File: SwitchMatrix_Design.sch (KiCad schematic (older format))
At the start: 0 parts

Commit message: v1b
Main notes -
Switch matrix added however not finished.
Minor notes -
Backspace is the only modified key to have been created so far.
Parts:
- added D? (x202): D_Small, symbol Device:D_Small
- added MX? (x202): MX-NoLED, symbol MX_Alps_Hybrid:MX-NoLED
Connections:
- net labels added: row0
- wire segments 0 -> 229

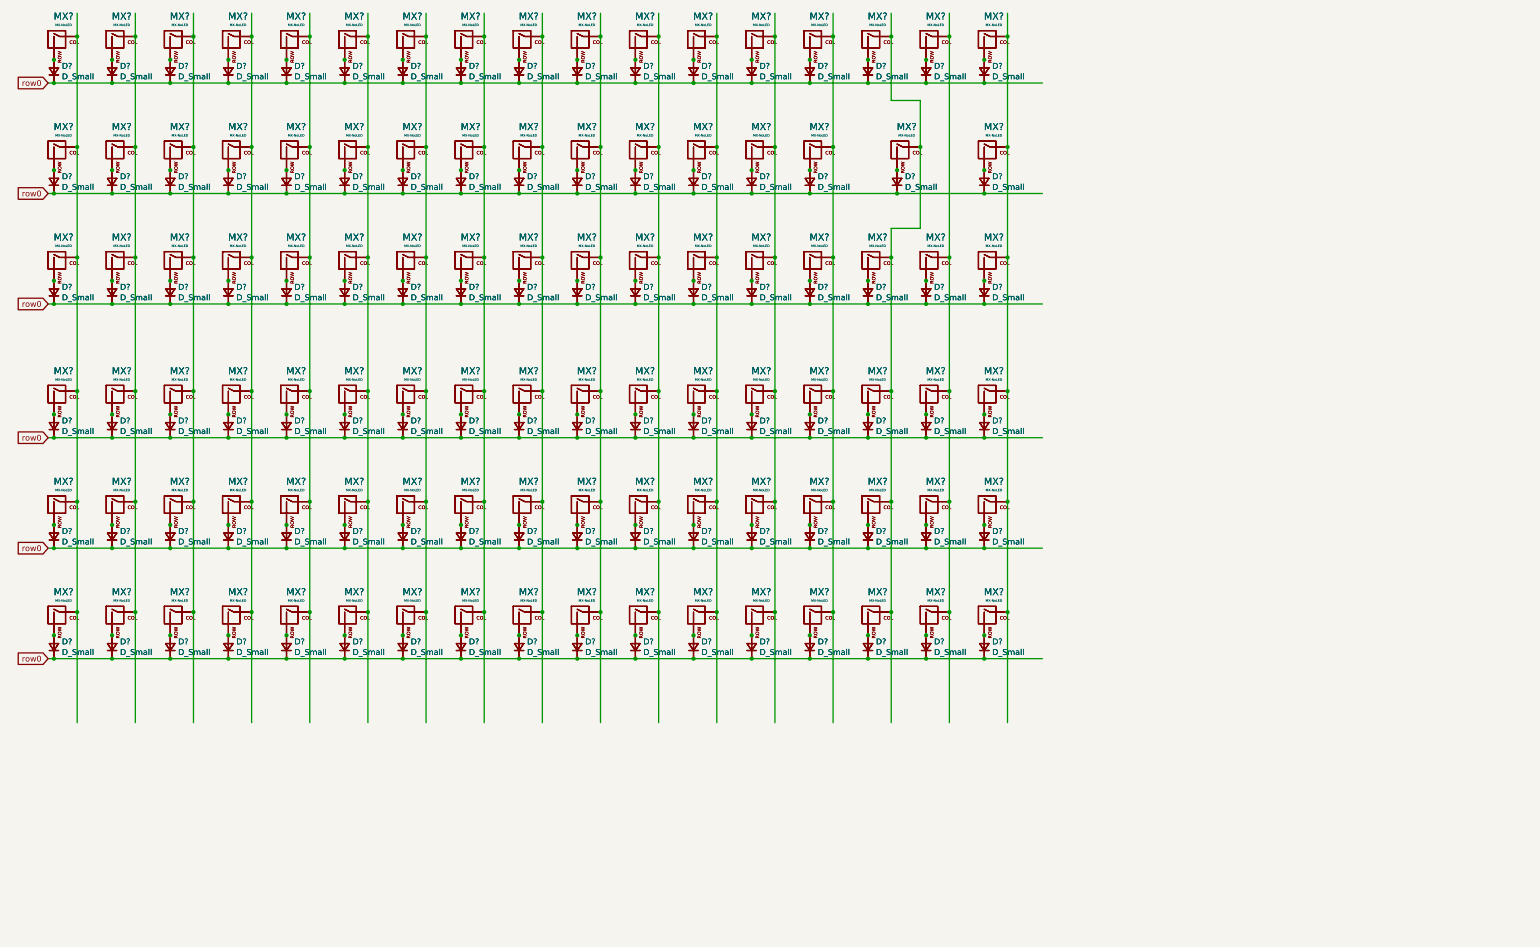
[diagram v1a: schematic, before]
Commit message: v1b2.2
Finished basic switch matrix layout.
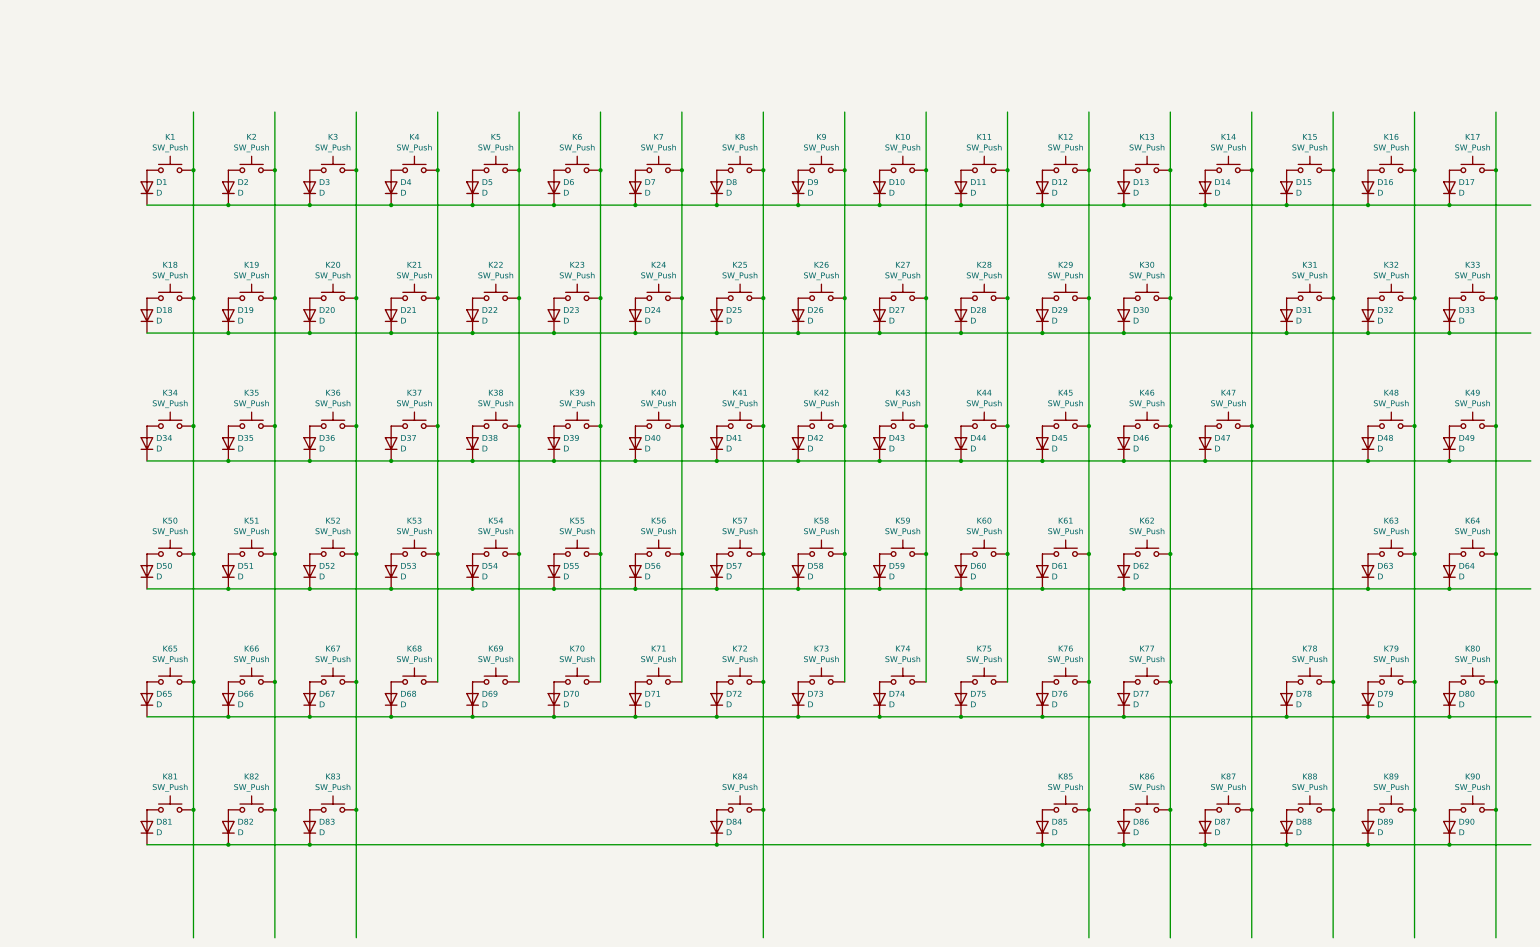
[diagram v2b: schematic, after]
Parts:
- removed D? (x202): D_Small, symbol Device:D_Small
- removed MX? (x202): MX-NoLED, symbol MX_Alps_Hybrid:MX-NoLED
- added D1, D10, D11, D12, D13, D14, D15, D16, D17, D18, D19, D2, D20, D21, D22, D23, D24, D25, D26, D27, D28, D29, D3, D30, D31, D32, D33, D34, D35, D36, D37, D38, D39, D4, D40, D41, D42, D43, D44, D45, D46, D47, D48, D49, D5, D50, D51, D52, D53, D54, D55, D56, D57, D58, D59, D6, D60, D61, D62, D63, D64, D65, D66, D67, D68, D69, D7, D70, D71, D72, D73, D74, D75, D76, D77, D78, D79, D8, D80, D81, D82, D83, D84, D85, D86, D87, D88, D89, D9, D90: D, symbol Device:D
- added K1, K10, K11, K12, K13, K14, K15, K16, K17, K18, K19, K2, K20, K21, K22, K23, K24, K25, K26, K27, K28, K29, K3, K30, K31, K32, K33, K34, K35, K36, K37, K38, K39, K4, K40, K41, K42, K43, K44, K45, K46, K47, K48, K49, K5, K50, K51, K52, K53, K54, K55, K56, K57, K58, K59, K6, K60, K61, K62, K63, K64, K65, K66, K67, K68, K69, K7, K70, K71, K72, K73, K74, K75, K76, K77, K78, K79, K8, K80, K81, K82, K83, K84, K85, K86, K87, K88, K89, K9, K90: SW_Push, symbol Switch:SW_Push
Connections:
- net labels removed: row0
- wire segments 229 -> 190
